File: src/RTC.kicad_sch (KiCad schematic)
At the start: 9 parts, among them U401 DS3231M

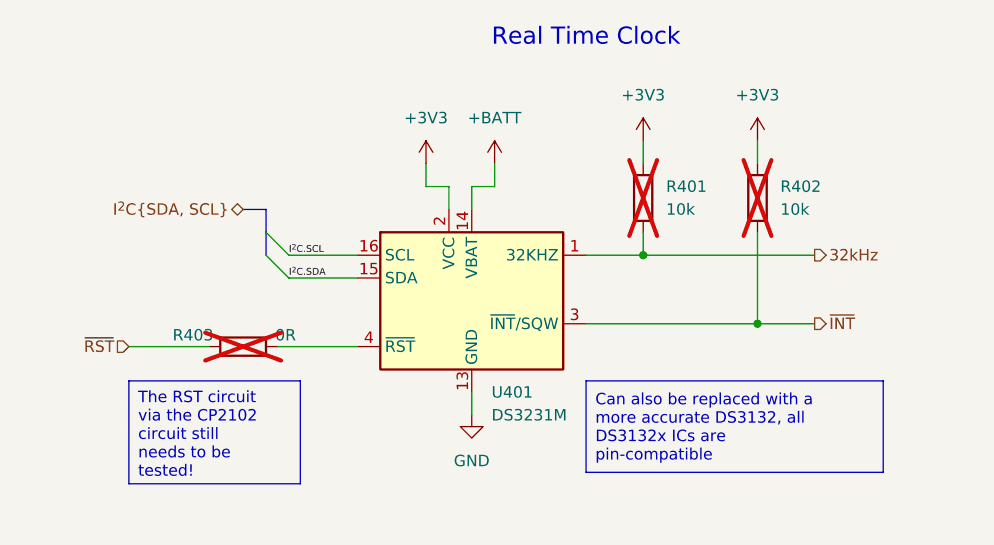
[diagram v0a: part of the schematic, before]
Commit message: Mod: Checked a few things and added the power limitation text to the LEDs page
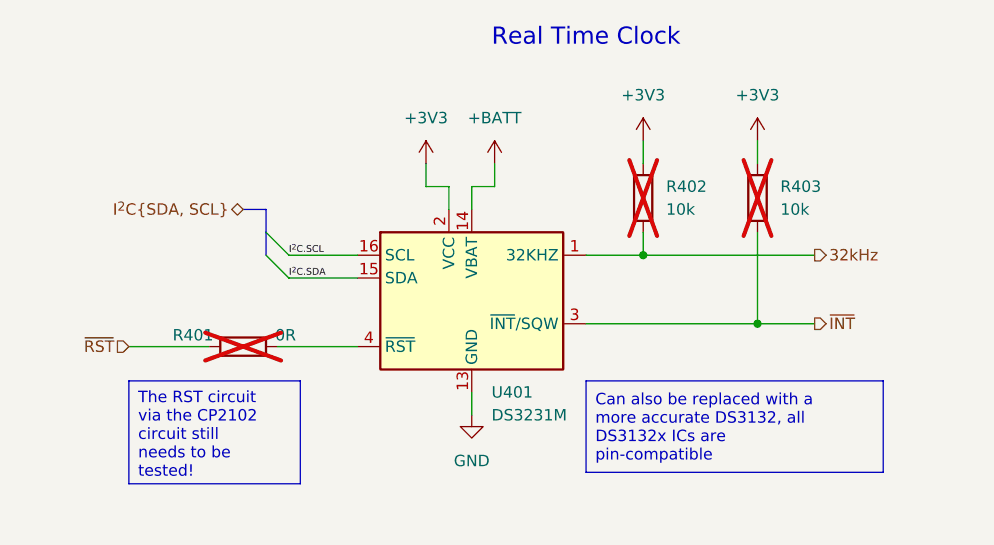
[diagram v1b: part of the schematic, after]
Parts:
- renumbered R403 to R401, R401 to R402, R402 to R403

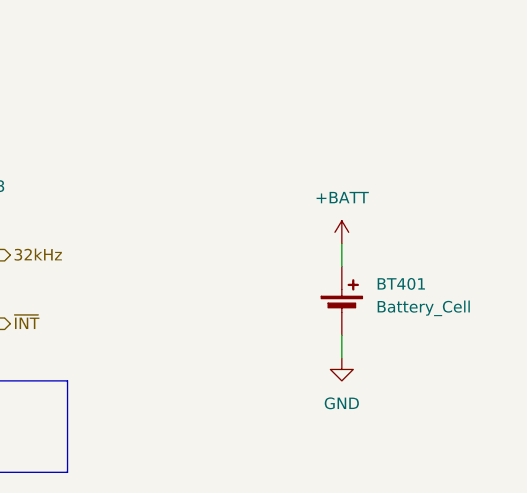
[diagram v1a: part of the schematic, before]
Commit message: Fix: Some errors from the ERC
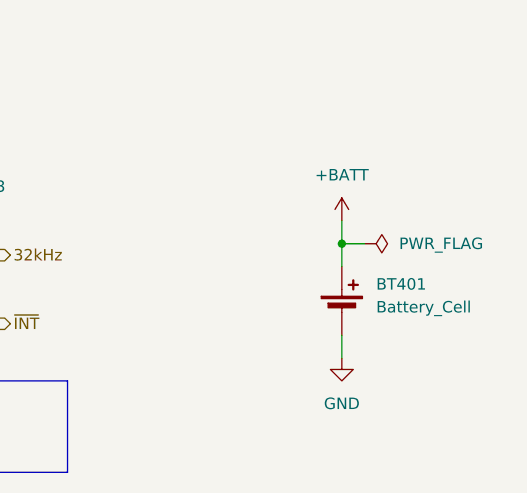
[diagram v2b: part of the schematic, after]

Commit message: Add: Vendor no. and footprints
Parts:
- BT401: footprint (none) -> Battery:BatteryHolder_Keystone_3002_1x2032; Manufacturer (none) -> Keystone Electronics; Manufacturer Part no. (none) -> 2898TR; Vendor 1 (none) -> Digikey; Vendor 1 Part no. (none) -> 36-2898CT-ND; Vendor 2 (none) -> LCSC; Vendor 2 Part no. (none) -> C6402533
- C401: footprint (none) -> Capacitor_SMD:C_0805_2012Metric_Pad1.18x1.45mm_HandSolder; Manufacturer (none) -> -; Manufacturer Part no. (none) -> -; Vendor 1 (none) -> Digikey; Vendor 1 Part no. (none) -> 1276-1096-1-ND; Vendor 2 (none) -> LCSC
- C402, C404: footprint (none) -> Capacitor_SMD:C_0805_2012Metric_Pad1.18x1.45mm_HandSolder; Manufacturer (none) -> -; Manufacturer Part no. (none) -> -; Vendor 1 (none) -> Digikey; Vendor 1 Part no. (none) -> 1276-2444-1-ND; Vendor 2 (none) -> LCSC
- C403: footprint (none) -> Capacitor_SMD:C_0805_2012Metric_Pad1.18x1.45mm_HandSolder; Manufacturer (none) -> -; Manufacturer Part no. (none) -> -; Vendor 1 (none) -> Digikey; Vendor 1 Part no. (none) -> 1276-1275-2-ND; Vendor 2 (none) -> LCSC
- R401: footprint (none) -> Resistor_SMD:R_0805_2012Metric_Pad1.20x1.40mm_HandSolder; Manufacturer (none) -> -; Manufacturer Part no. (none) -> -; Vendor 1 (none) -> Digikey; Vendor 1 Part no. (none) -> 311-0.0ARCT-ND; Vendor 2 (none) -> LCSC
- R402, R403: footprint (none) -> Resistor_SMD:R_0805_2012Metric_Pad1.20x1.40mm_HandSolder; Manufacturer (none) -> -; Manufacturer Part no. (none) -> -; Vendor 1 (none) -> Digikey; Vendor 1 Part no. (none) -> 311-10.0KCRCT-ND; Vendor 2 (none) -> LCSC
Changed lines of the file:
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@@
 			)
 		)
-		(property "Footprint" ""
+		(property "Footprint" "Capacitor_SMD:C_0805_2012Metric_Pad1.18x1.45mm_HandSolder"
 			(at 166.0652 181.61 0)
 			(effects
@@
 			)
 		)
-		(property "Manufacturer" ""
+		(property "Manufacturer" "-"
 			(at 165.1 177.8 0)
 			(effects
@@
 			)
 		)
-		(property "Manufacturer Part no." ""
+		(property "Manufacturer Part no." "-"
 			(at 165.1 177.8 0)
 			(effects
@@
 			)
 		)
-		(property "Vendor 1" ""
+		(property "Vendor 1" "Digikey"
 			(at 165.1 177.8 0)
 			(effects
@@
 			)
 		)
-		(property "Vendor 1 Part no." ""
+		(property "Vendor 1 Part no." "1276-2444-1-ND "
 			(at 165.1 177.8 0)
 			(effects
@@
 			)
 		)
-		(property "Vendor 2" ""
+		(property "Vendor 2" "LCSC"
 			(at 165.1 177.8 0)
 			(effects
@@
 			)
 		)
-		(property "Footprint" ""
+		(property "Footprint" "Battery:BatteryHolder_Keystone_3002_1x2032"
 			(at 190.5 86.106 90)
 			(effects
@@
 		)
 		(property "Sim.Type" ""
+			(at 190.5 87.63 0)
+			(effects
+				(font
+					(size 1.27 1.27)
+				)
+				(hide yes)
+			)
+		)
+		(property "Vendor 1" "Digikey"
+			(at 190.5 87.63 0)
+			(effects
+				(font
+					(size 1.27 1.27)
+				)
+				(hide yes)
+			)
+		)
+		(property "Vendor 2" "LCSC"
+			(at 190.5 87.63 0)
+			(effects
+				(font
+					(size 1.27 1.27)
+				)
+				(hide yes)
+			)
+		)
+		(property "Manufacturer" "Keystone Electronics"
+			(at 190.5 87.63 0)
+			(effects
+				(font
+					(size 1.27 1.27)
+				)
+				(hide yes)
+			)
+		)
+		(property "Manufacturer Part no." "2898TR"
+			(at 190.5 87.63 0)
+			(effects
+				(font
+					(size 1.27 1.27)
+				)
+				(hide yes)
+			)
+		)
+		(property "Vendor 1 Part no." "36-2898CT-ND"
+			(at 190.5 87.63 0)
+			(effects
+				(font
+					(size 1.27 1.27)
+				)
+				(hide yes)
+			)
+		)
+		(property "Vendor 2 Part no." "C6402533"
 			(at 190.5 87.63 0)
 			(effects
@@
 			)
 		)
-		(property "Footprint" ""
+		(property "Footprint" "Resistor_SMD:R_0805_2012Metric_Pad1.20x1.40mm_HandSolder"
 			(at 144.272 74.93 90)
 			(effects
@@
 			)
 		)
-		(property "Manufacturer" ""
+		(property "Manufacturer" "-"
 			(at 146.05 74.93 0)
 			(effects
@@
 			)
 		)
-		(property "Manufacturer Part no." ""
+		(property "Manufacturer Part no." "-"
 			(at 146.05 74.93 0)
 			(effects
@@
 			)
 		)
-		(property "Vendor 1" ""
+		(property "Vendor 1" "Digikey"
 			(at 146.05 74.93 0)
 			(effects
@@
 			)
 		)
-		(property "Vendor 1 Part no." ""
+		(property "Vendor 1 Part no." "311-10.0KCRCT-ND"
 			(at 146.05 74.93 0)
 			(effects
@@
 			)
 		)
-		(property "Vendor 2" ""
+		(property "Vendor 2" "LCSC"
 			(at 146.05 74.93 0)
 			(effects
@@
 			)
 		)
-		(property "Footprint" ""
+		(property "Footprint" "Capacitor_SMD:C_0805_2012Metric_Pad1.18x1.45mm_HandSolder"
 			(at 26.3652 181.61 0)
 			(effects
@@
 		)
 		(property "Sim.Type" ""
+			(at 25.4 177.8 0)
+			(effects
+				(font
+					(size 1.27 1.27)
+				)
+				(hide yes)
+			)
+		)
+		(property "Manufacturer" "-"
+			(at 25.4 177.8 0)
+			(effects
+				(font
+					(size 1.27 1.27)
+				)
+				(hide yes)
+			)
+		)
+		(property "Manufacturer Part no." "-"
+			(at 25.4 177.8 0)
+			(effects
+				(font
+					(size 1.27 1.27)
+				)
+				(hide yes)
+			)
+		)
+		(property "Vendor 1" "Digikey"
+			(at 25.4 177.8 0)
+			(effects
+				(font
+					(size 1.27 1.27)
+				)
+				(hide yes)
+			)
+		)
+		(property "Vendor 1 Part no." "1276-1096-1-ND"
+			(at 25.4 177.8 0)
+			(effects
+				(font
+					(size 1.27 1.27)
+				)
+				(hide yes)
+			)
+		)
+		(property "Vendor 2" "LCSC"
 			(at 25.4 177.8 0)
 			(effects
@@
 			)
 		)
-		(property "Footprint" ""
+		(property "Footprint" "Resistor_SMD:R_0805_2012Metric_Pad1.20x1.40mm_HandSolder"
 			(at 131.572 74.93 90)
 			(effects
@@
 			)
 		)
-		(property "Manufacturer" ""
+		(property "Manufacturer" "-"
 			(at 133.35 74.93 0)
 			(effects
@@
 			)
 		)
-		(property "Manufacturer Part no." ""
+		(property "Manufacturer Part no." "-"
 			(at 133.35 74.93 0)
 			(effects
@@
 			)
 		)
-		(property "Vendor 1" ""
+		(property "Vendor 1" "Digikey"
 			(at 133.35 74.93 0)
 			(effects
@@
 			)
 		)
-		(property "Vendor 1 Part no." ""
+		(property "Vendor 1 Part no." "311-10.0KCRCT-ND"
 			(at 133.35 74.93 0)
 			(effects
@@
 			)
 		)
-		(property "Vendor 2" ""
+		(property "Vendor 2" "LCSC"
 			(at 133.35 74.93 0)
 			(effects
@@
 			)
 		)
-		(property "Footprint" ""
+		(property "Footprint" "Resistor_SMD:R_0805_2012Metric_Pad1.20x1.40mm_HandSolder"
 			(at 88.9 89.662 90)
 			(effects
@@
 			)
 		)
-		(property "Manufacturer" ""
+		(property "Manufacturer" "-"
 			(at 88.9 91.44 0)
 			(effects
@@
 			)
 		)
-		(property "Manufacturer Part no." ""
+		(property "Manufacturer Part no." "-"
 			(at 88.9 91.44 0)
 			(effects
@@
 			)
 		)
-		(property "Vendor 1" ""
+		(property "Vendor 1" "Digikey"
 			(at 88.9 91.44 0)
 			(effects
@@
 			)
 		)
-		(property "Vendor 1 Part no." ""
+		(property "Vendor 1 Part no." "311-0.0ARCT-ND"
 			(at 88.9 91.44 0)
 			(effects
@@
 			)
 		)
-		(property "Vendor 2" ""
+		(property "Vendor 2" "LCSC"
 			(at 88.9 91.44 0)
 			(effects
@@
 			)
 		)
-		(property "Footprint" ""
+		(property "Footprint" "Capacitor_SMD:C_0805_2012Metric_Pad1.18x1.45mm_HandSolder"
 			(at 153.3652 181.61 0)
 			(effects
@@
 			)
 		)
-		(property "Manufacturer" ""
+		(property "Manufacturer" "-"
 			(at 152.4 177.8 0)
 			(effects
@@
 			)
 		)
-		(property "Manufacturer Part no." ""
+		(property "Manufacturer Part no." "-"
 			(at 152.4 177.8 0)
 			(effects
@@
 			)
 		)
-		(property "Vendor 1" ""
+		(property "Vendor 1" "Digikey"
 			(at 152.4 177.8 0)
 			(effects
@@
 			)
 		)
-		(property "Vendor 1 Part no." ""
+		(property "Vendor 1 Part no." "1276-1275-2-ND"
 			(at 152.4 177.8 0)
 			(effects
@@
 			)
 		)
-		(property "Vendor 2" ""
+		(property "Vendor 2" "LCSC"
 			(at 152.4 177.8 0)
 			(effects
@@
 			)
 		)
-		(property "Footprint" ""
+		(property "Footprint" "Capacitor_SMD:C_0805_2012Metric_Pad1.18x1.45mm_HandSolder"
 			(at 39.0652 181.61 0)
 			(effects
@@
 			(at 38.1 177.8 0)
 			(effects
+				(font
+					(size 1.27 1.27)
+				)
+				(hide yes)
+			)
+		)
+		(property "Manufacturer" "-"
+			(at 38.1 177.8 0)
+			(effects
+				(font
+					(size 1.27 1.27)
+				)
+				(hide yes)
+			)
+		)
+		(property "Manufacturer Part no." "-"
+			(at 38.1 177.8 0)
+			(effects
+				(font
+					(size 1.27 1.27)
+				)
+				(hide yes)
+			)
+		)
+		(property "Vendor 1" "Digikey"
+			(at 38.1 177.8 0)
+			(effects
+				(font
+					(size 1.27 1.27)
+				)
+				(hide yes)
+			)
+		)
+		(property "Vendor 1 Part no." "1276-2444-1-ND "
+			(at 38.1 177.8 0)
+			(effects
+				(font
+					(size 1.27 1.27)
+				)
+				(hide yes)
+			)
+		)
+		(property "Vendor 2" "LCSC"
+			(at 38.1 177.8 0)
+			(effects

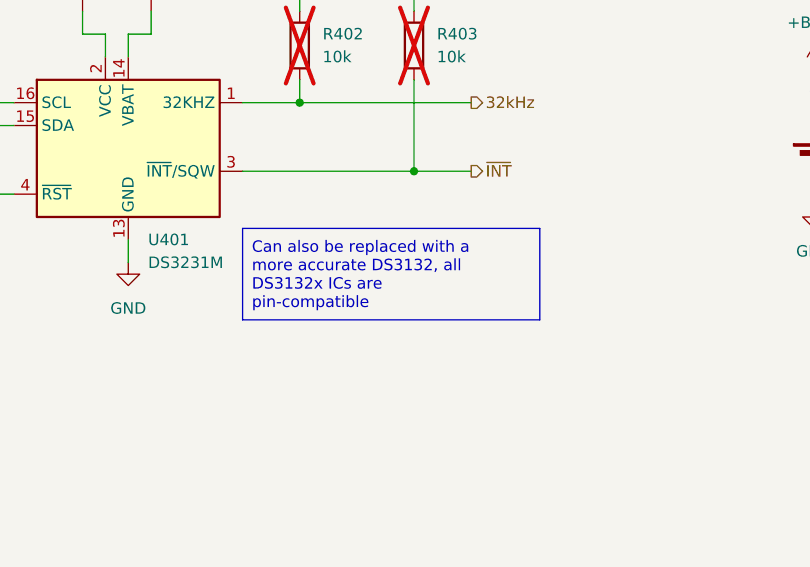
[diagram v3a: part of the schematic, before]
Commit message: Mod: Changed parts to match with both vendors
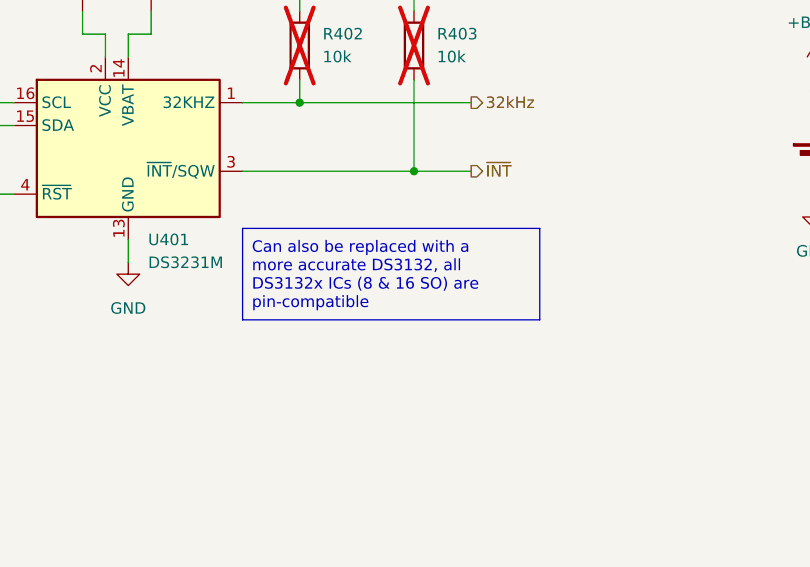
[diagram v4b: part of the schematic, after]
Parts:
- BT401: Manufacturer Part no. 2898TR -> 2898; Vendor 1 Part no. 36-2898CT-ND -> 36-2898-ND; Vendor 2 Part no. C6402533 -> C6379018
- C401: Manufacturer - -> Samsung Electro-Mechanics; Manufacturer Part no. - -> CL21A106KOQNNNE; Vendor 2 Part no. (none) -> C1713
- C402, C404: Manufacturer - -> Samsung Electro-Mechanics; Manufacturer Part no. - -> CL21B104KBCNFNC; Vendor 2 Part no. (none) -> C318718
- C403: Manufacturer - -> Samsung Electro-Mechanics; Manufacturer Part no. - -> CL21B105KPFNNNE; Vendor 2 Part no. (none) -> C107367
- R401: Manufacturer - -> YAGEO; Manufacturer Part no. - -> RC0805JR-070RL; Vendor 2 Part no. (none) -> C96345
- R402, R403: Manufacturer - -> YAGEO; Manufacturer Part no. - -> RC0805FR-0710KL; Vendor 2 Part no. (none) -> C84376
- U401: Comment (none) -> LCSC, only has the 8 pin variant; Vendor 2 Part no. C107410 (8-pin variant!) -> C107410
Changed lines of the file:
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@@
 	(title_block
 		(title "Wordclock - Real Time Clock")
-		(date "2024-10-27")
+		(date "2024-10-29")
 		(rev "A")
 		(company "ElektroNik Zoller")
@@
 		)
 	)
-	(text_box "Can also be replaced with a more accurate DS3132, all DS3132x ICs are pin-compatible"
+	(text_box "Can also be replaced with a more accurate DS3132, all DS3132x ICs (8 & 16 SO) are pin-compatible"
 		(exclude_from_sim no)
 		(at 127 95.25 0)
@@
 			)
 		)
-		(property "Manufacturer" "-"
+		(property "Manufacturer" "Samsung Electro-Mechanics"
 			(at 165.1 177.8 0)
 			(effects
@@
 			)
 		)
-		(property "Manufacturer Part no." "-"
+		(property "Manufacturer Part no." "CL21B104KBCNFNC"
 			(at 165.1 177.8 0)
 			(effects
@@
 			)
 		)
-		(property "Vendor 2 Part no." ""
+		(property "Vendor 2 Part no." "C318718"
 			(at 165.1 177.8 0)
 			(effects
@@
 			)
 		)
-		(property "Manufacturer Part no." "2898TR"
+		(property "Manufacturer Part no." "2898"
 			(at 190.5 87.63 0)
 			(effects
@@
 			)
 		)
-		(property "Vendor 1 Part no." "36-2898CT-ND"
+		(property "Vendor 1 Part no." "36-2898-ND"
 			(at 190.5 87.63 0)
 			(effects
@@
 			)
 		)
-		(property "Vendor 2 Part no." "C6402533"
+		(property "Vendor 2 Part no." "C6379018"
 			(at 190.5 87.63 0)
 			(effects
@@
 			)
 		)
-		(property "Manufacturer" "-"
+		(property "Manufacturer" "YAGEO"
 			(at 146.05 74.93 0)
 			(effects
@@
 			)
 		)
-		(property "Manufacturer Part no." "-"
+		(property "Manufacturer Part no." "RC0805FR-0710KL"
 			(at 146.05 74.93 0)
 			(effects
@@
 			)
 		)
-		(property "Vendor 2 Part no." ""
+		(property "Vendor 2 Part no." "C84376"
 			(at 146.05 74.93 0)
 			(effects
@@
 			)
 		)
-		(property "Manufacturer" "-"
+		(property "Manufacturer" "Samsung Electro-Mechanics"
 			(at 25.4 177.8 0)
 			(effects
@@
 			)
 		)
-		(property "Manufacturer Part no." "-"
+		(property "Manufacturer Part no." "CL21A106KOQNNNE"
 			(at 25.4 177.8 0)
 			(effects
@@
 		)
 		(property "Vendor 2" "LCSC"
+			(at 25.4 177.8 0)
+			(effects
+				(font
+					(size 1.27 1.27)
+				)
+				(hide yes)
+			)
+		)
+		(property "Vendor 2 Part no." "C1713"
 			(at 25.4 177.8 0)
 			(effects
@@
 			)
 		)
-		(property "Manufacturer" "-"
+		(property "Manufacturer" "YAGEO"
 			(at 133.35 74.93 0)
 			(effects
@@
 			)
 		)
-		(property "Manufacturer Part no." "-"
+		(property "Manufacturer Part no." "RC0805FR-0710KL"
 			(at 133.35 74.93 0)
 			(effects
@@
 			)
 		)
-		(property "Vendor 2 Part no." ""
+		(property "Vendor 2 Part no." "C84376"
 			(at 133.35 74.93 0)
 			(effects
@@
 			)
 		)
-		(property "Manufacturer" "-"
+		(property "Manufacturer" "YAGEO"
 			(at 88.9 91.44 0)
 			(effects
@@
 			)
 		)
-		(property "Manufacturer Part no." "-"
+		(property "Manufacturer Part no." "RC0805JR-070RL"
 			(at 88.9 91.44 0)
 			(effects
@@
 			)
 		)
-		(property "Vendor 2 Part no." ""
+		(property "Vendor 2 Part no." "C96345"
 			(at 88.9 91.44 0)
 			(effects
@@
 			)
 		)
-		(property "Vendor 2 Part no." " C107410 (8-pin variant!)"
+		(property "Vendor 2 Part no." "C107410"
 			(at 114.3 86.36 0)
 			(effects
@@
 		)
 		(property "Sim.Type" ""
+			(at 114.3 86.36 0)
+			(effects
+				(font
+					(size 1.27 1.27)
+				)
+				(hide yes)
+			)
+		)
+		(property "Comment" "LCSC, only has the 8 pin variant"
 			(at 114.3 86.36 0)
 			(effects
@@
 			)
 		)
-		(property "Manufacturer" "-"
+		(property "Manufacturer" "Samsung Electro-Mechanics"
 			(at 152.4 177.8 0)
 			(effects
@@
 			)
 		)
-		(property "Manufacturer Part no." "-"
+		(property "Manufacturer Part no." "CL21B105KPFNNNE"
 			(at 152.4 177.8 0)
 			(effects
@@
 			)
 		)
-		(property "Vendor 2 Part no." ""
+		(property "Vendor 2 Part no." "C107367"
 			(at 152.4 177.8 0)
 			(effects
@@
 			)
 		)
-		(property "Manufacturer" "-"
+		(property "Manufacturer" "Samsung Electro-Mechanics"
 			(at 38.1 177.8 0)
 			(effects
@@
 			)
 		)
-		(property "Manufacturer Part no." "-"
+		(property "Manufacturer Part no." "CL21B104KBCNFNC"
 			(at 38.1 177.8 0)
 			(effects
@@
 			(at 38.1 177.8 0)
 			(effects
+				(font
+					(size 1.27 1.27)
+				)
+				(hide yes)
+			)
+		)
+		(property "Vendor 2 Part no." "C318718"
+			(at 38.1 177.8 0)
+			(effects

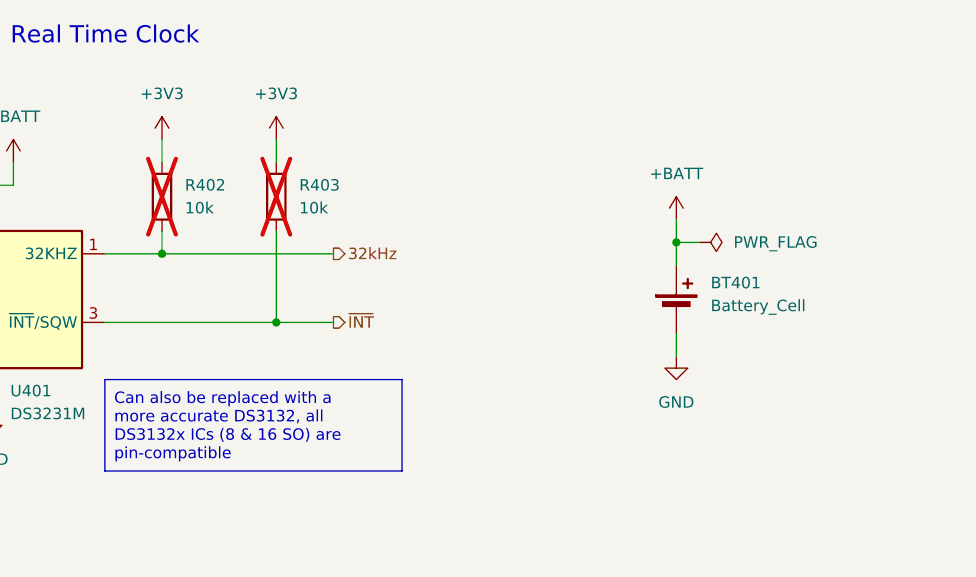
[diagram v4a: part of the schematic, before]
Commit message: Add: Header for empty pins of the ESP32 and added more 0R resistors to break up some connections
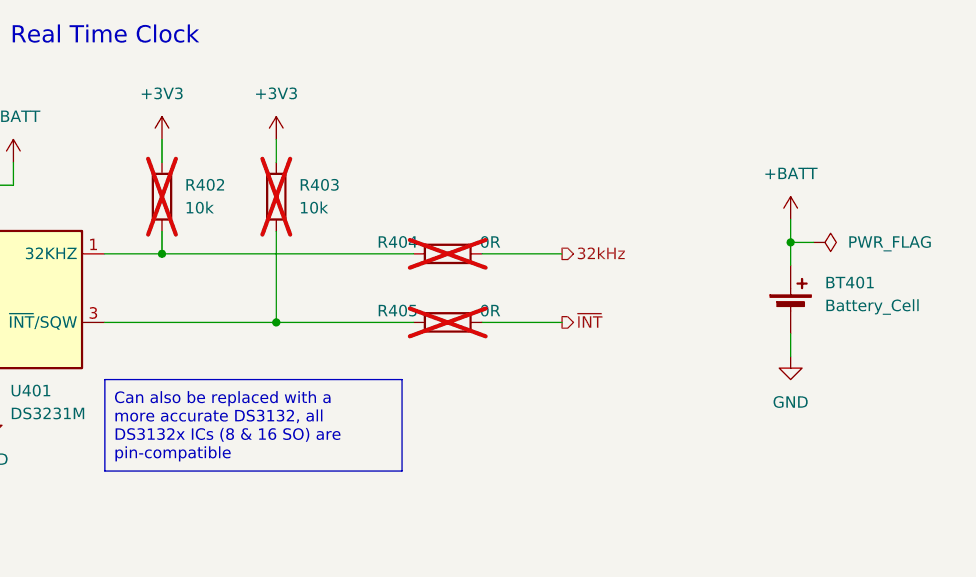
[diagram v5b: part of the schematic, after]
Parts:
- added R404, R405: 0R, Resistor_SMD:R_0805_2012Metric_Pad1.20x1.40mm_HandSolder, symbol Device:R
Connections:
- net 32kHz: now also R404.1; no longer R402.2, U401.1 (32KHZ)
- net ~{INT}: now also R405.1; no longer R403.2, U401.3 (~{INT}/SQW)
- new net: R403.2, R405.2, U401.3 (~{INT}/SQW)
- new net: R402.2, R404.2, U401.1 (32KHZ)
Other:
- moved on the sheet: BT401

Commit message: Fix: Name of the battery cell. Run ERC and created finished schematic, ready for the layout
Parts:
- BT401: value Battery_Cell -> CR2032
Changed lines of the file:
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@@
 			)
 		)
-		(property "Value" "Battery_Cell"
+		(property "Value" "CR2032"
 			(at 207.01 87.0584 0)
 			(effects
